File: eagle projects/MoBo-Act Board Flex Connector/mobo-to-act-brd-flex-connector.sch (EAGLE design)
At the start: 2 parts

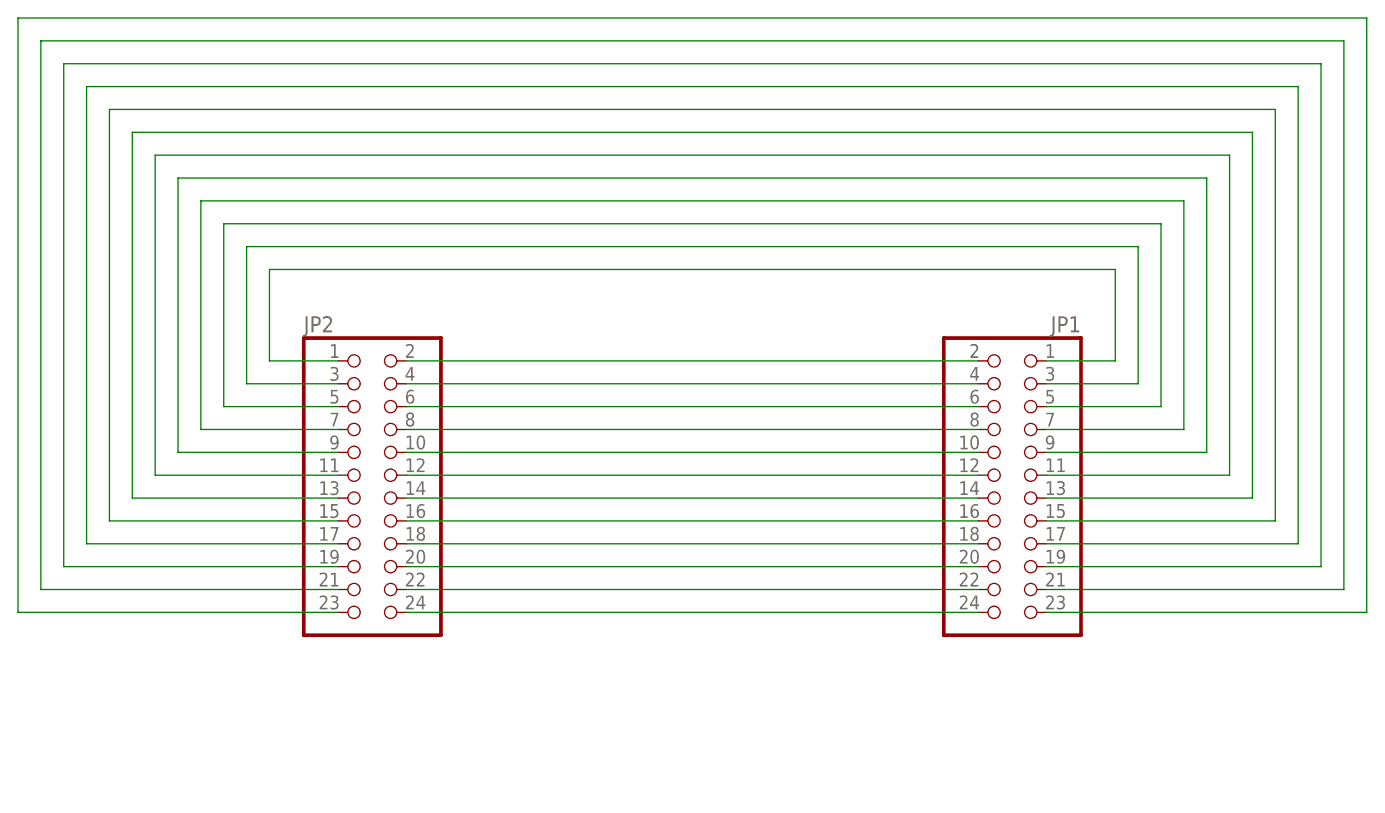
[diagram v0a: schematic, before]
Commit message: Added 24 pin SMD header and lengthened both connectors
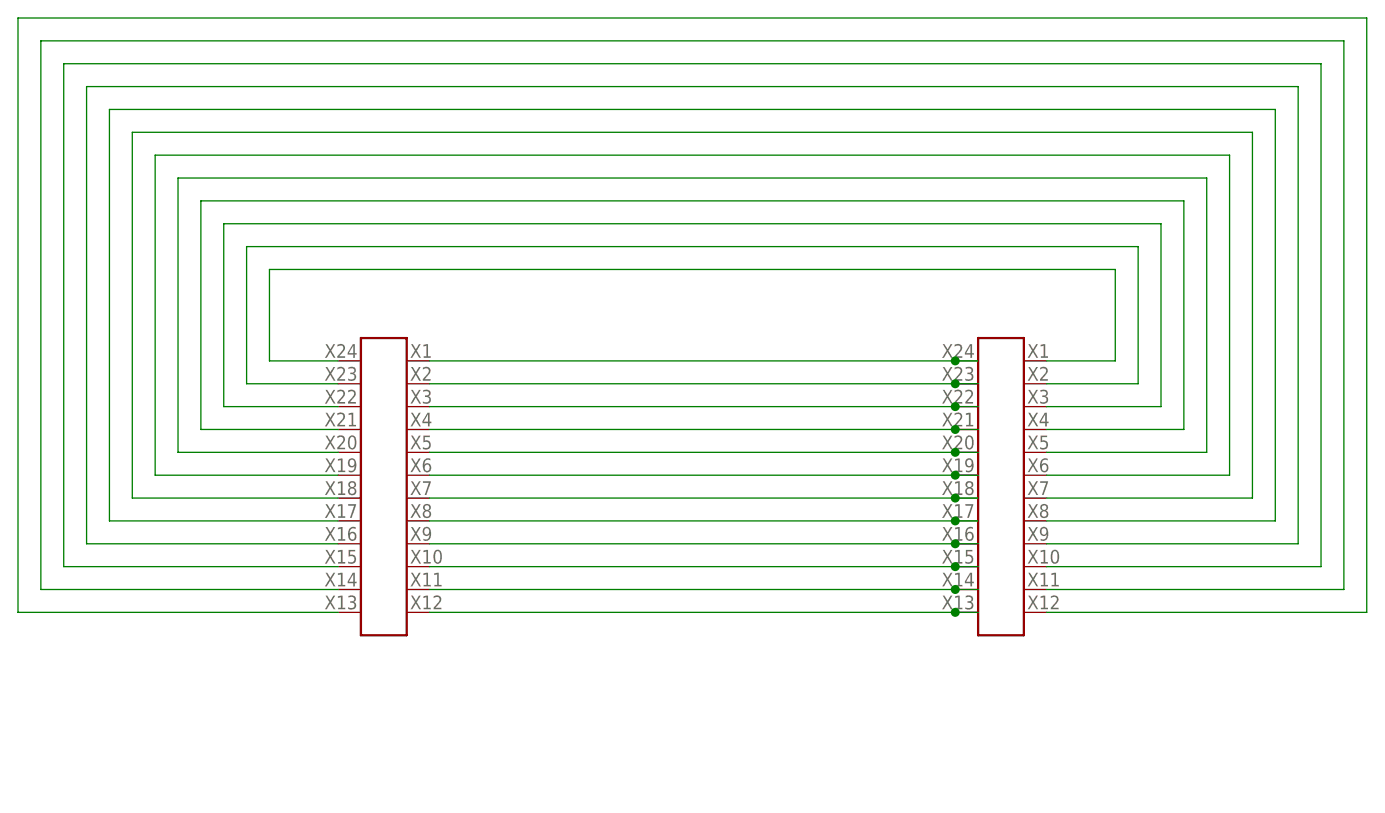
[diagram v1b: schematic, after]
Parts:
- removed JP1, JP2: (no value), pinhead:PINHD-2X12
- added U$1, U$2: 12X2_SMD_2.54MM_HEADER, SMD_headers:12X2_SMD_2.54MM_HEADER
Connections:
- net N$1: now also U$1.P$1, U$2.P$24; no longer JP1.2, JP2.2
- net N$10: now also U$1.P$10, U$2.P$15; no longer JP1.20, JP2.20
- net N$11: now also U$1.P$11, U$2.P$14; no longer JP1.22, JP2.22
- net N$12: now also U$1.P$12, U$2.P$13; no longer JP1.24, JP2.24
- net N$13: now also U$1.P$24, U$2.P$1; no longer JP1.1, JP2.1
- net N$14: now also U$1.P$23, U$2.P$2; no longer JP1.3, JP2.3
- net N$15: now also U$1.P$22, U$2.P$3; no longer JP1.5, JP2.5
- net N$16: now also U$1.P$21, U$2.P$4; no longer JP1.7, JP2.7
- net N$17: now also U$1.P$20, U$2.P$5; no longer JP1.9, JP2.9
- net N$18: now also U$1.P$19, U$2.P$6; no longer JP1.11, JP2.11
- net N$19: now also U$1.P$18, U$2.P$7; no longer JP1.13, JP2.13
- net N$2: now also U$1.P$2, U$2.P$23; no longer JP1.4, JP2.4
- net N$20: now also U$1.P$17, U$2.P$8; no longer JP1.15, JP2.15
- net N$21: now also U$1.P$16, U$2.P$9; no longer JP1.17, JP2.17
- net N$22: now also U$1.P$15, U$2.P$10; no longer JP1.19, JP2.19
- net N$23: now also U$1.P$14, U$2.P$11; no longer JP1.21, JP2.21
- net N$24: now also U$1.P$13, U$2.P$12; no longer JP1.23, JP2.23
- net N$3: now also U$1.P$3, U$2.P$22; no longer JP1.6, JP2.6
- net N$4: now also U$1.P$4, U$2.P$21; no longer JP1.8, JP2.8
- net N$5: now also U$1.P$5, U$2.P$20; no longer JP1.10, JP2.10
- net N$6: now also U$1.P$6, U$2.P$19; no longer JP1.12, JP2.12
- net N$7: now also U$1.P$7, U$2.P$18; no longer JP1.14, JP2.14
- net N$8: now also U$1.P$8, U$2.P$17; no longer JP1.16, JP2.16
- net N$9: now also U$1.P$9, U$2.P$16; no longer JP1.18, JP2.18

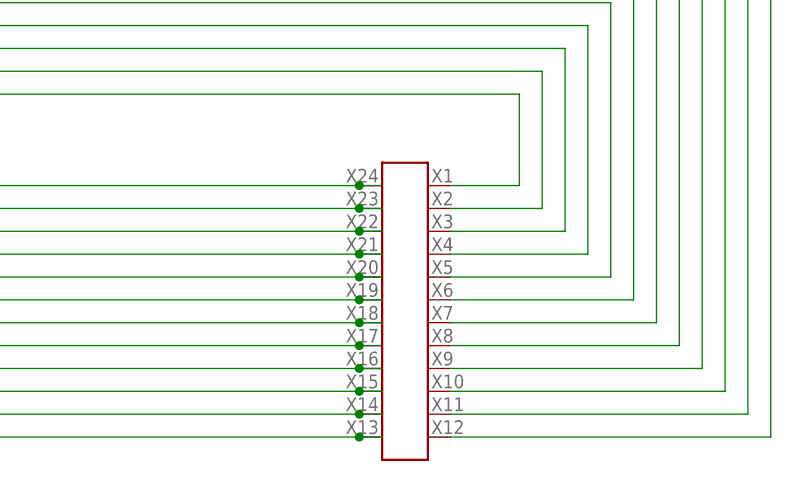
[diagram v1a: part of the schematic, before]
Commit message: Mirrored one of the connectors ends (incorrectly)
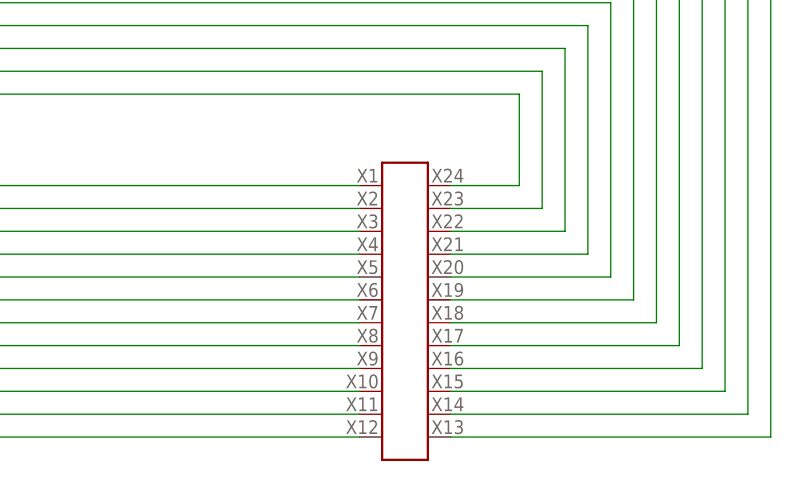
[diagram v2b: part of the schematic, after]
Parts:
- U$2: value 12X2_SMD_2.54MM_HEADER -> 12X2_MIRRORED_SMD_2.54MM_HEADER; device SMD_headers:12X2_SMD_2.54MM_HEADER -> SMD_headers:12X2_MIRRORED_SMD_2.54MM_HEADER
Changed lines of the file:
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@@
 <parts>
 <part name="FRAME1" library="my_library" library_urn="urn:adsk.eagle:library:22876504" deviceset="TITLE_BLOCK_LETTER" device=""/>
-<part name="U$2" library="SMD_headers" deviceset="12X2_SMD_2.54MM_HEADER" device=""/>
 <part name="U$1" library="SMD_headers" deviceset="12X2_SMD_2.54MM_HEADER" device=""/>
+<part name="U$2" library="SMD_headers" deviceset="12X2_MIRRORED_SMD_2.54MM_HEADER" device=""/>
 </parts>
 <sheets>
@@
 <attribute name="DRAWING_NAME" x="190.5" y="19.05" size="2.54" layer="94"/>
 </instance>
+<instance part="U$1" gate="G$1" x="124.46" y="121.92" smashed="yes"/>
 <instance part="U$2" gate="G$1" x="193.04" y="121.92" smashed="yes"/>
-<instance part="U$1" gate="G$1" x="124.46" y="121.92" smashed="yes"/>
 </instances>
 <busses>
@@
 <segment>
 <wire x1="104.14" y1="132.08" x2="162.56" y2="132.08" width="0.1524" layer="91"/>
+<pinref part="U$1" gate="G$1" pin="P$1"/>
 <pinref part="U$2" gate="G$1" pin="P$24"/>
-<wire x1="162.56" y1="132.08" x2="165.1" y2="132.08" width="0.1524" layer="91"/>
-<junction x="162.56" y="132.08"/>
-<pinref part="U$1" gate="G$1" pin="P$1"/>
 </segment>
 </net>
@@
 <segment>
 <wire x1="104.14" y1="129.54" x2="162.56" y2="129.54" width="0.1524" layer="91"/>
+<pinref part="U$1" gate="G$1" pin="P$2"/>
 <pinref part="U$2" gate="G$1" pin="P$23"/>
-<wire x1="162.56" y1="129.54" x2="165.1" y2="129.54" width="0.1524" layer="91"/>
-<junction x="162.56" y="129.54"/>
-<pinref part="U$1" gate="G$1" pin="P$2"/>
 </segment>
 </net>
@@
 <segment>
 <wire x1="104.14" y1="127" x2="162.56" y2="127" width="0.1524" layer="91"/>
+<pinref part="U$1" gate="G$1" pin="P$3"/>
 <pinref part="U$2" gate="G$1" pin="P$22"/>
-<wire x1="162.56" y1="127" x2="165.1" y2="127" width="0.1524" layer="91"/>
-<junction x="162.56" y="127"/>
-<pinref part="U$1" gate="G$1" pin="P$3"/>
 </segment>
 </net>
@@
 <segment>
 <wire x1="104.14" y1="124.46" x2="162.56" y2="124.46" width="0.1524" layer="91"/>
+<pinref part="U$1" gate="G$1" pin="P$4"/>
 <pinref part="U$2" gate="G$1" pin="P$21"/>
-<wire x1="162.56" y1="124.46" x2="165.1" y2="124.46" width="0.1524" layer="91"/>
-<junction x="162.56" y="124.46"/>
-<pinref part="U$1" gate="G$1" pin="P$4"/>
 </segment>
 </net>
@@
 <segment>
 <wire x1="104.14" y1="121.92" x2="162.56" y2="121.92" width="0.1524" layer="91"/>
+<pinref part="U$1" gate="G$1" pin="P$5"/>
 <pinref part="U$2" gate="G$1" pin="P$20"/>
-<wire x1="162.56" y1="121.92" x2="165.1" y2="121.92" width="0.1524" layer="91"/>
-<junction x="162.56" y="121.92"/>
-<pinref part="U$1" gate="G$1" pin="P$5"/>
 </segment>
 </net>
@@
 <segment>
 <wire x1="104.14" y1="119.38" x2="162.56" y2="119.38" width="0.1524" layer="91"/>
+<pinref part="U$1" gate="G$1" pin="P$6"/>
 <pinref part="U$2" gate="G$1" pin="P$19"/>
-<wire x1="162.56" y1="119.38" x2="165.1" y2="119.38" width="0.1524" layer="91"/>
-<junction x="162.56" y="119.38"/>
-<pinref part="U$1" gate="G$1" pin="P$6"/>
 </segment>
 </net>
@@
 <segment>
 <wire x1="104.14" y1="116.84" x2="162.56" y2="116.84" width="0.1524" layer="91"/>
+<pinref part="U$1" gate="G$1" pin="P$7"/>
 <pinref part="U$2" gate="G$1" pin="P$18"/>
-<wire x1="162.56" y1="116.84" x2="165.1" y2="116.84" width="0.1524" layer="91"/>
-<junction x="162.56" y="116.84"/>
-<pinref part="U$1" gate="G$1" pin="P$7"/>
 </segment>
 </net>
@@
 <segment>
 <wire x1="104.14" y1="114.3" x2="162.56" y2="114.3" width="0.1524" layer="91"/>
+<pinref part="U$1" gate="G$1" pin="P$8"/>
 <pinref part="U$2" gate="G$1" pin="P$17"/>
-<wire x1="162.56" y1="114.3" x2="165.1" y2="114.3" width="0.1524" layer="91"/>
-<junction x="162.56" y="114.3"/>
-<pinref part="U$1" gate="G$1" pin="P$8"/>
 </segment>
 </net>
@@
 <segment>
 <wire x1="104.14" y1="111.76" x2="162.56" y2="111.76" width="0.1524" layer="91"/>
+<pinref part="U$1" gate="G$1" pin="P$9"/>
 <pinref part="U$2" gate="G$1" pin="P$16"/>
-<wire x1="162.56" y1="111.76" x2="165.1" y2="111.76" width="0.1524" layer="91"/>
-<junction x="162.56" y="111.76"/>
-<pinref part="U$1" gate="G$1" pin="P$9"/>
 </segment>
 </net>
@@
 <segment>
 <wire x1="104.14" y1="109.22" x2="162.56" y2="109.22" width="0.1524" layer="91"/>
+<pinref part="U$1" gate="G$1" pin="P$10"/>
 <pinref part="U$2" gate="G$1" pin="P$15"/>
-<wire x1="162.56" y1="109.22" x2="165.1" y2="109.22" width="0.1524" layer="91"/>
-<junction x="162.56" y="109.22"/>
-<pinref part="U$1" gate="G$1" pin="P$10"/>
 </segment>
 </net>
@@
 <segment>
 <wire x1="104.14" y1="106.68" x2="162.56" y2="106.68" width="0.1524" layer="91"/>
+<pinref part="U$1" gate="G$1" pin="P$11"/>
 <pinref part="U$2" gate="G$1" pin="P$14"/>
-<wire x1="162.56" y1="106.68" x2="165.1" y2="106.68" width="0.1524" layer="91"/>
-<junction x="162.56" y="106.68"/>
-<pinref part="U$1" gate="G$1" pin="P$11"/>
 </segment>
 </net>
@@
 <segment>
 <wire x1="104.14" y1="104.14" x2="162.56" y2="104.14" width="0.1524" layer="91"/>
+<pinref part="U$1" gate="G$1" pin="P$12"/>
 <pinref part="U$2" gate="G$1" pin="P$13"/>
-<wire x1="162.56" y1="104.14" x2="165.1" y2="104.14" width="0.1524" layer="91"/>
-<junction x="162.56" y="104.14"/>
-<pinref part="U$1" gate="G$1" pin="P$12"/>
 </segment>
 </net>
@@
 <wire x1="180.34" y1="142.24" x2="180.34" y2="132.08" width="0.1524" layer="91"/>
 <wire x1="180.34" y1="132.08" x2="172.72" y2="132.08" width="0.1524" layer="91"/>
+<pinref part="U$1" gate="G$1" pin="P$24"/>
 <pinref part="U$2" gate="G$1" pin="P$1"/>
-<pinref part="U$1" gate="G$1" pin="P$24"/>
 </segment>
 </net>
@@
 <wire x1="182.88" y1="144.78" x2="182.88" y2="129.54" width="0.1524" layer="91"/>
 <wire x1="182.88" y1="129.54" x2="172.72" y2="129.54" width="0.1524" layer="91"/>
+<pinref part="U$1" gate="G$1" pin="P$23"/>
 <pinref part="U$2" gate="G$1" pin="P$2"/>
-<pinref part="U$1" gate="G$1" pin="P$23"/>
 </segment>
 </net>
@@
 <wire x1="185.42" y1="147.32" x2="185.42" y2="127" width="0.1524" layer="91"/>
 <wire x1="185.42" y1="127" x2="172.72" y2="127" width="0.1524" layer="91"/>
+<pinref part="U$1" gate="G$1" pin="P$22"/>
 <pinref part="U$2" gate="G$1" pin="P$3"/>
-<pinref part="U$1" gate="G$1" pin="P$22"/>
 </segment>
 </net>
@@
 <wire x1="187.96" y1="149.86" x2="187.96" y2="124.46" width="0.1524" layer="91"/>
 <wire x1="187.96" y1="124.46" x2="172.72" y2="124.46" width="0.1524" layer="91"/>
+<pinref part="U$1" gate="G$1" pin="P$21"/>
 <pinref part="U$2" gate="G$1" pin="P$4"/>
-<pinref part="U$1" gate="G$1" pin="P$21"/>
 </segment>
 </net>
@@
 <wire x1="190.5" y1="152.4" x2="190.5" y2="121.92" width="0.1524" layer="91"/>
 <wire x1="190.5" y1="121.92" x2="172.72" y2="121.92" width="0.1524" layer="91"/>
+<pinref part="U$1" gate="G$1" pin="P$20"/>
 <pinref part="U$2" gate="G$1" pin="P$5"/>
-<pinref part="U$1" gate="G$1" pin="P$20"/>
 </segment>
 </net>
@@
 <wire x1="193.04" y1="154.94" x2="193.04" y2="119.38" width="0.1524" layer="91"/>
 <wire x1="193.04" y1="119.38" x2="172.72" y2="119.38" width="0.1524" layer="91"/>
+<pinref part="U$1" gate="G$1" pin="P$19"/>
 <pinref part="U$2" gate="G$1" pin="P$6"/>
-<pinref part="U$1" gate="G$1" pin="P$19"/>
 </segment>
 </net>
@@
 <wire x1="195.58" y1="157.48" x2="195.58" y2="116.84" width="0.1524" layer="91"/>
 <wire x1="195.58" y1="116.84" x2="172.72" y2="116.84" width="0.1524" layer="91"/>
+<pinref part="U$1" gate="G$1" pin="P$18"/>
 <pinref part="U$2" gate="G$1" pin="P$7"/>
-<pinref part="U$1" gate="G$1" pin="P$18"/>
 </segment>
 </net>
@@
 <wire x1="198.12" y1="160.02" x2="198.12" y2="114.3" width="0.1524" layer="91"/>
 <wire x1="198.12" y1="114.3" x2="172.72" y2="114.3" width="0.1524" layer="91"/>
+<pinref part="U$1" gate="G$1" pin="P$17"/>
 <pinref part="U$2" gate="G$1" pin="P$8"/>
-<pinref part="U$1" gate="G$1" pin="P$17"/>
 </segment>
 </net>
@@
 <wire x1="200.66" y1="162.56" x2="200.66" y2="111.76" width="0.1524" layer="91"/>
 <wire x1="200.66" y1="111.76" x2="172.72" y2="111.76" width="0.1524" layer="91"/>
+<pinref part="U$1" gate="G$1" pin="P$16"/>
 <pinref part="U$2" gate="G$1" pin="P$9"/>
-<pinref part="U$1" gate="G$1" pin="P$16"/>
 </segment>
 </net>
@@
 <wire x1="203.2" y1="165.1" x2="203.2" y2="109.22" width="0.1524" layer="91"/>
 <wire x1="203.2" y1="109.22" x2="172.72" y2="109.22" width="0.1524" layer="91"/>
+<pinref part="U$1" gate="G$1" pin="P$15"/>
 <pinref part="U$2" gate="G$1" pin="P$10"/>
-<pinref part="U$1" gate="G$1" pin="P$15"/>
 </segment>
 </net>
@@
 <wire x1="205.74" y1="167.64" x2="205.74" y2="106.68" width="0.1524" layer="91"/>
 <wire x1="205.74" y1="106.68" x2="172.72" y2="106.68" width="0.1524" layer="91"/>
+<pinref part="U$1" gate="G$1" pin="P$14"/>
 <pinref part="U$2" gate="G$1" pin="P$11"/>
-<pinref part="U$1" gate="G$1" pin="P$14"/>
 </segment>
 </net>
@@
 <wire x1="208.28" y1="170.18" x2="208.28" y2="104.14" width="0.1524" layer="91"/>
 <wire x1="208.28" y1="104.14" x2="172.72" y2="104.14" width="0.1524" layer="91"/>
+<pinref part="U$1" gate="G$1" pin="P$13"/>
 <pinref part="U$2" gate="G$1" pin="P$12"/>
-<pinref part="U$1" gate="G$1" pin="P$13"/>
-</segment>
-</net>
+</segment>
+</net>
